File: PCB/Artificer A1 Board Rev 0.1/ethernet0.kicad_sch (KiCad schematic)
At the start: 33 parts, among them J2 LPJG0926HENL, J4 PoE, U8 RTL8211F-CG, X2 25MHz

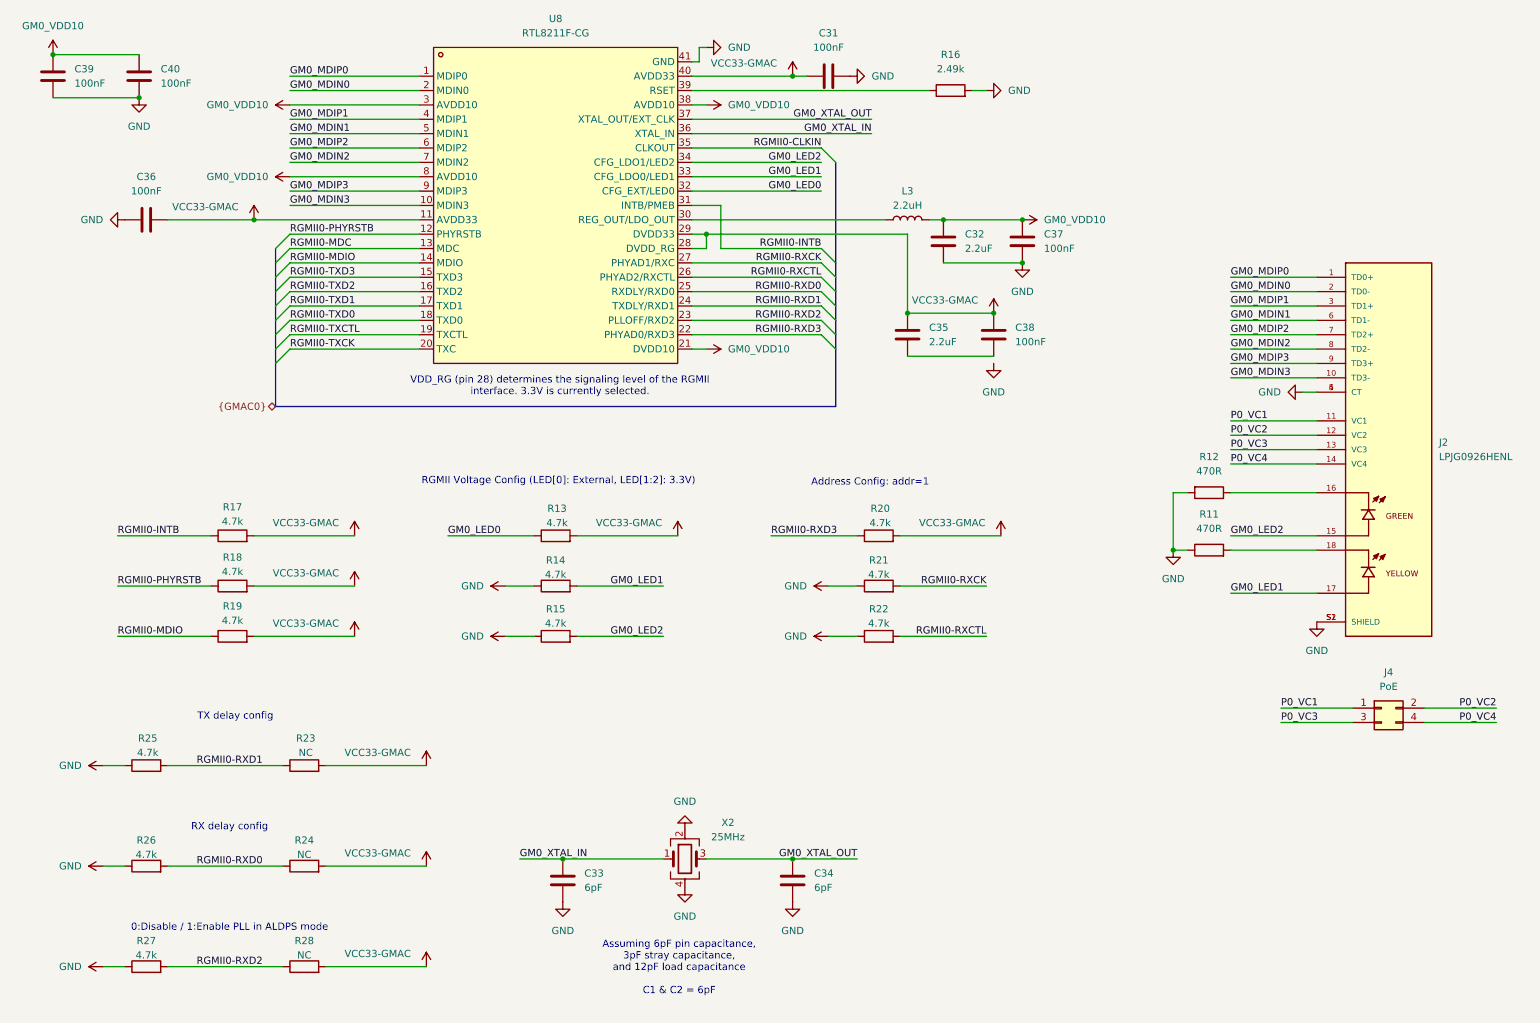
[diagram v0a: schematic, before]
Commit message: cleaned up, kicad 10 & usb c pd
migrated to Kicad 10,
added USB PD for power input
added capacitors inductors and resistor footprints
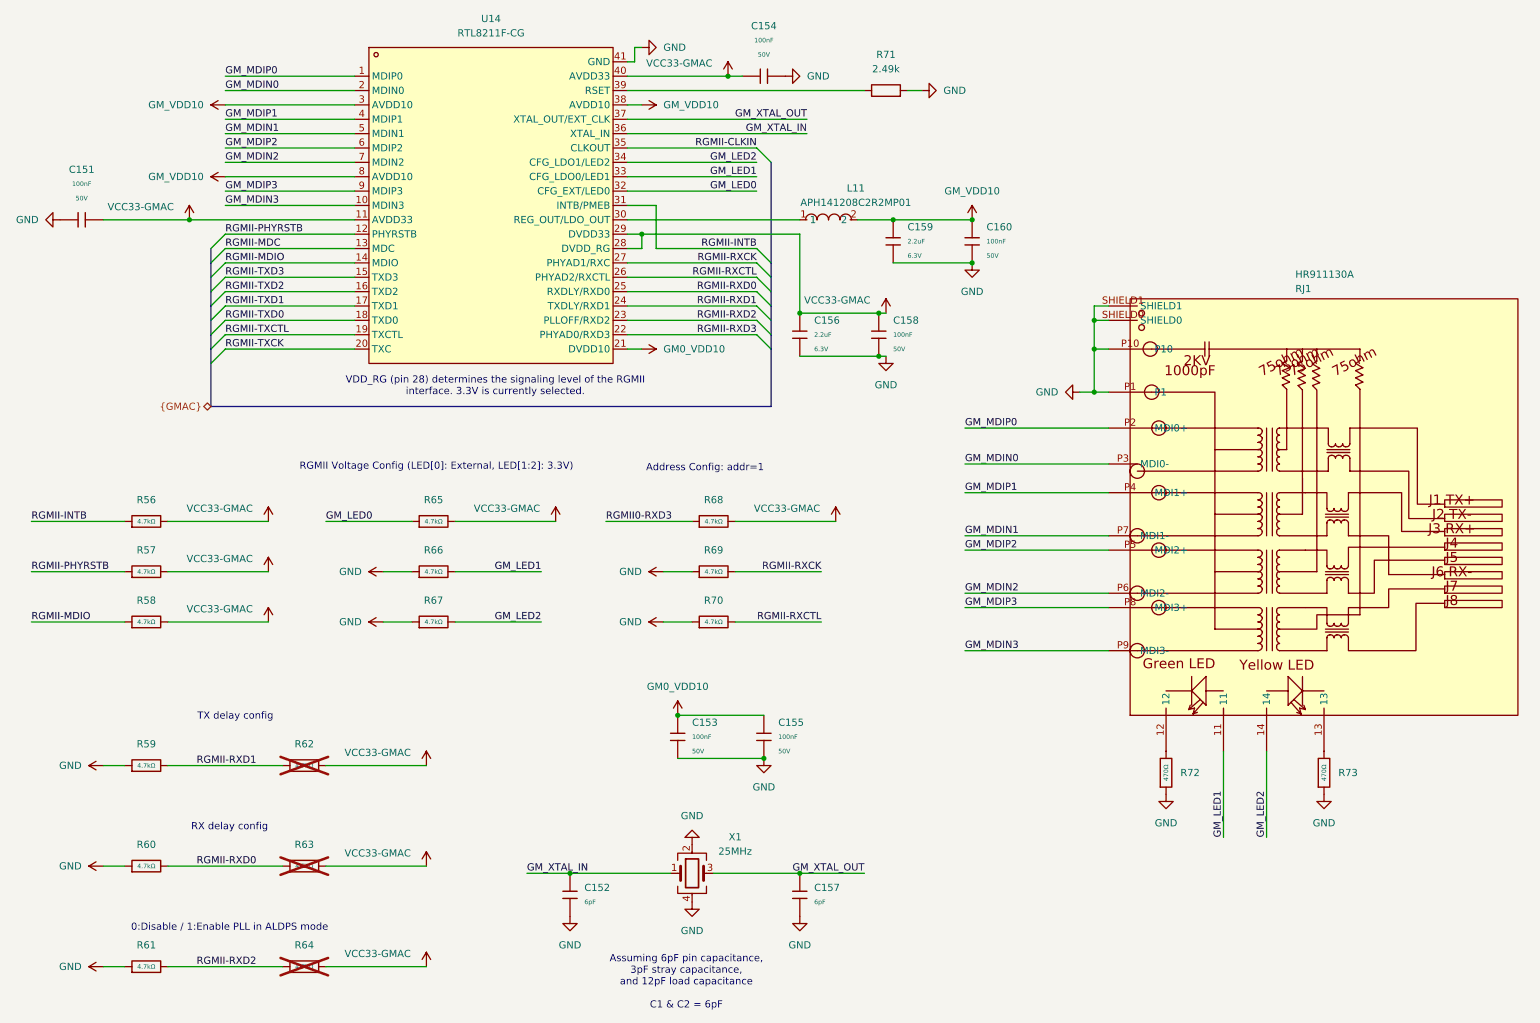
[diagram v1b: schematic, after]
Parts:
- removed C31, C36, C37, C38, C39, C40: 100nF, symbol Device:C
- removed C32, C35: 2.2uF, symbol Device:C
- removed C33, C34: 6pF, symbol Device:C
- removed J2: LPJG0926HENL, custom footprints:LINK-PP_LPJG0926HENL, symbol LPJG0926HENL:LPJG0926HENL
- removed J4: PoE, Connector_PinHeader_2.54mm:PinHeader_2x02_P2.54mm_Vertical, symbol Connector_Generic:Conn_02x02_Odd_Even
- removed L3: 2.2uH, symbol Device:L
- removed R11, R12: 470R, symbol Device:R
- removed R13, R14, R15, R17, R18, R19, R20, R21, R22, R25, R26, R27: 4.7k, symbol Device:R
- removed R23, R24, R28: NC, symbol Device:R
- added C151, C153, C154, C155, C158, C160: 100nF, PCM_JLCPCB:C_0402, symbol PCM_JLCPCB-Capacitors:0402,100nF,(2)
- added C152, C157: 6pF, PCM_JLCPCB:C_0402, symbol PCM_JLCPCB-Capacitors:0402,6pF
- added C156, C159: 2.2uF, PCM_JLCPCB:C_0402, symbol PCM_JLCPCB-Capacitors:0402,2.2uF
- added L11: APH141208C2R2MP01, easyeda:IND-SMD_L1.4-W1.2_AOTA-B141206SR47MT, symbol easyeda:APH141208C2R2MP01
- added R56, R57, R58, R59, R60, R61, R62, R63, R64, R65, R66, R67, R68, R69, R70: 4.7kΩ, PCM_JLCPCB:R_0402, symbol PCM_JLCPCB-Resistors:0402,4.7kΩ
- added R72, R73: 470Ω, PCM_JLCPCB:R_0402, symbol PCM_JLCPCB-Resistors:0402,470Ω
- added RJ1: HR911130A, easyeda:RJ45-TH_HR911130A, symbol easyeda:HR911130A
- R71: renamed from R16; footprint (none) -> PCM_JLCPCB:R_0402; LCSC (none) -> C2933083
- renumbered U8 to U14, X2 to X1
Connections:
- net GM0_VDD10: now also C153.1, C155.1; no longer U14.3 (AVDD10), U14.38 (AVDD10), U14.8 (AVDD10)
- net GND: now also C151.1, C152.2, C153.2, C154.2, C155.2, C156.2, C157.2, C158.2, C159.2, C160.2, R59.1, R60.1, R61.1, R66.1, R67.1, R69.1, R70.1, R72.1, R73.1, RJ1.P1, RJ1.P10, RJ1.SHIELD0, RJ1.SHIELD1
- net RGMII0-RXD3: now also R68.1; no longer U14.22 (PHYAD0/RXD3)
- net VCC33-GMAC: now also C151.2, C154.1, C156.1, C158.1, R56.2, R57.2, R58.2, R62.2, R63.2, R64.2, R65.2, R68.2
- net at U14.30 (REG_OUT/LDO_OUT): now also L11.1
- net GM0_LED0 renamed GM_LED0
- net GM_LED0: now also R65.1
- net GM0_LED1 renamed GM_LED1
- net GM_LED1: now also R66.2, RJ1.11
- net GM0_LED2 renamed GM_LED2
- net GM_LED2: now also R67.2, RJ1.14
- net GM0_MDIN0 renamed GM_MDIN0
- net GM_MDIN0: now also RJ1.P3 (MDI0-)
- net GM0_MDIN1 renamed GM_MDIN1
- net GM_MDIN1: now also RJ1.P7 (MDI1-)
- net GM0_MDIN2 renamed GM_MDIN2
- net GM_MDIN2: now also RJ1.P6 (MDI2-)
- net GM0_MDIN3 renamed GM_MDIN3
- net GM_MDIN3: now also RJ1.P9 (MDI3-)
- net GM0_MDIP0 renamed GM_MDIP0
- net GM_MDIP0: now also RJ1.P2 (MDI0+)
- net GM0_MDIP1 renamed GM_MDIP1
- net GM_MDIP1: now also RJ1.P4 (MDI1+)
- net GM0_MDIP2 renamed GM_MDIP2
- net GM_MDIP2: now also RJ1.P5 (MDI2+)
- net GM0_MDIP3 renamed GM_MDIP3
- net GM_MDIP3: now also RJ1.P8 (MDI3+)
- net GM0_XTAL_IN renamed GM_XTAL_IN
- net GM_XTAL_IN: now also C152.1
- net GM0_XTAL_OUT renamed GM_XTAL_OUT
- net GM_XTAL_OUT: now also C157.1
- net RGMII0-CLKIN renamed RGMII-CLKIN
- net RGMII0-INTB renamed RGMII-INTB
- net RGMII-INTB: now also R56.1
- net RGMII0-MDC renamed RGMII-MDC
- net RGMII0-MDIO renamed RGMII-MDIO
- net RGMII-MDIO: now also R58.1
- net RGMII0-PHYRSTB renamed RGMII-PHYRSTB
- net RGMII-PHYRSTB: now also R57.1
- net RGMII0-RXCK renamed RGMII-RXCK
- net RGMII-RXCK: now also R69.2
- net RGMII0-RXCTL renamed RGMII-RXCTL
- net RGMII-RXCTL: now also R70.2
- net RGMII0-RXD0 renamed RGMII-RXD0
- net RGMII-RXD0: now also R60.2, R63.1
- net RGMII0-RXD1 renamed RGMII-RXD1
- net RGMII-RXD1: now also R59.2, R62.1
- net RGMII0-RXD2 renamed RGMII-RXD2
- net RGMII-RXD2: now also R61.2, R64.1
- net RGMII0-TXCK renamed RGMII-TXCK
- net RGMII0-TXCTL renamed RGMII-TXCTL
- net RGMII0-TXD0 renamed RGMII-TXD0
- net RGMII0-TXD1 renamed RGMII-TXD1
- net RGMII0-TXD2 renamed RGMII-TXD2
- net RGMII0-TXD3 renamed RGMII-TXD3
- new net: R72.2, RJ1.12
- new net: R73.2, RJ1.13
- new net GM_VDD10: C159.1, C160.1, L11.2, U14.3 (AVDD10), U14.38 (AVDD10), U14.8 (AVDD10)
- new net RGMII-RXD3: U14.22 (PHYAD0/RXD3)
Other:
- moved on the sheet: R71, U14, X1
